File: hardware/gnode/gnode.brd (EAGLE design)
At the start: 50 x 35 mm, 8 parts, among them U1 ATMEGA328P_TQFP, U2 3.3V/150mA

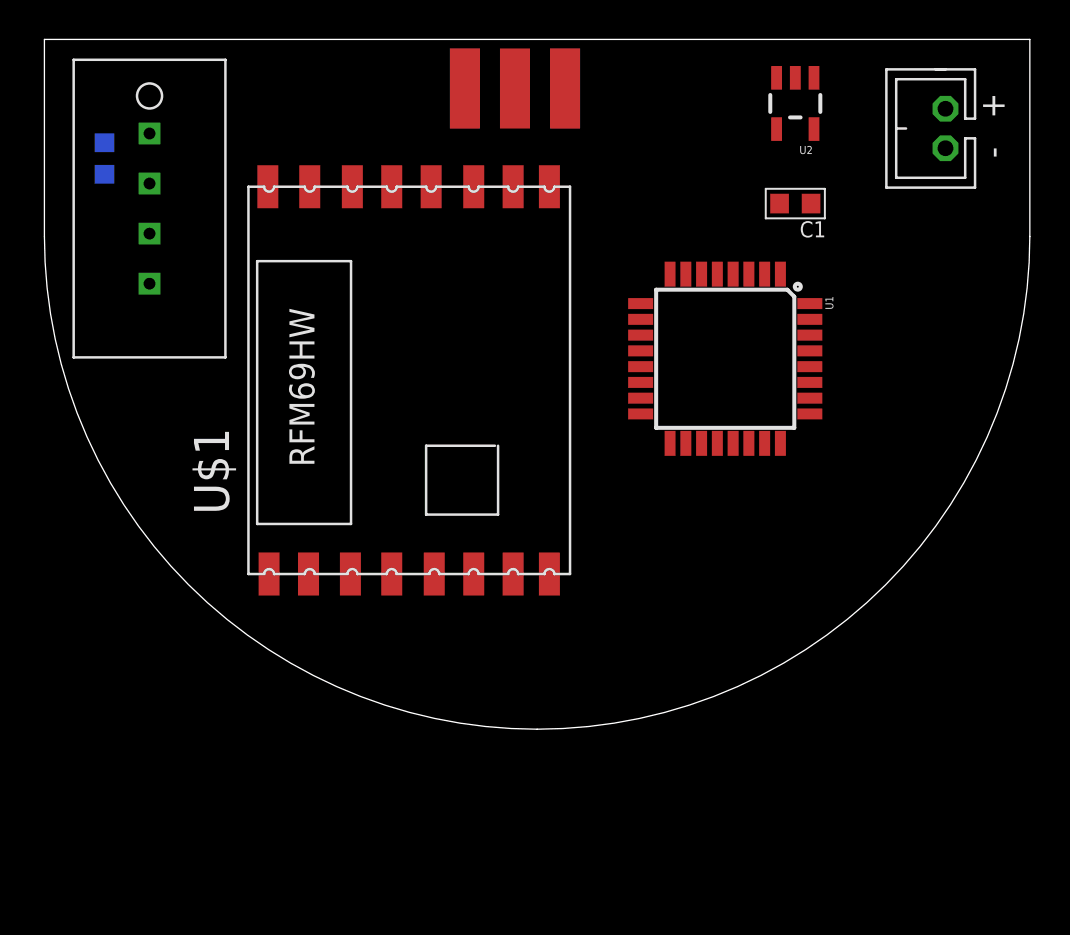
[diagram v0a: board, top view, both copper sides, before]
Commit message: reduced to r25mm, added htu21d and icsp header
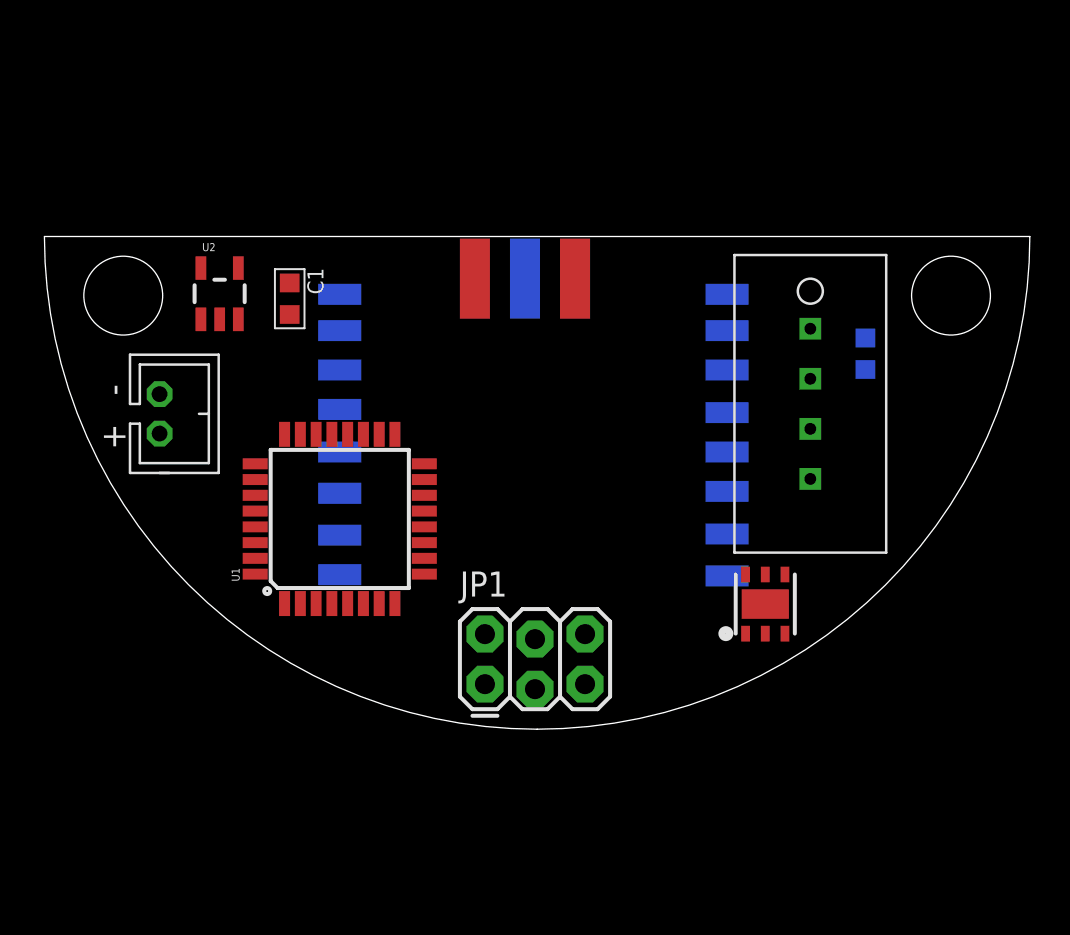
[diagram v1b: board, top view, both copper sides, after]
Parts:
- added IC1: HTU21D, Mine:DFN6-L
- added JP1: AVR_SPI_PRG_62X3_LOCK, SparkFun-Connectors:2X3_LOCK
- moved J1 42.4 mm to (5.84, 16.0), turned to 270 degrees
- moved R1 39.9 mm to (41.7, 19.1)
- moved U$2 35.0 mm to (38.9, 16.5)
- moved U2 30.8 mm to (8.89, 22.1), turned to 0 degrees
- moved C1 26.1 mm to (12.4, 21.8), turned to 270 degrees
- moved U1 21.2 mm to (15.0, 10.7), turned to 90 degrees
- moved U$1 19.2 mm to (15.0, 23.1), flipped to the bottom, turned to 180 degrees
- moved J$1 11.2 mm to (26.9, 22.9), flipped to the bottom
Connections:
- new net NRST: JP1.5, U1.29
- new net SHT_DATA: IC1.1, U1.27
- new net SHT_SCK: IC1.6, U1.28
- net GND: now also IC1.2, JP1.6
- net MISO: now also JP1.1
- net MOSI: now also JP1.4
- net SCK: now also JP1.3
- net VCC: now also JP1.2
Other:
- board size 50 x 35 mm -> 50 x 25 mm

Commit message: switched to mcp1700
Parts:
- removed U2: 3.3V/150mA, SparkFun-PowerIC:SOT23-5
- added C2: 1u, passives-7351:C0603-N
- added U$3: MCP1700TT, dtb:SOT23
- C1: value (none) -> 1u
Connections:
- net GND: now also C2.2, U$3.1; no longer U2.2
- net N$2: now also C2.1, U$3.3; no longer U2.1, U2.3
- net VCC: now also U$3.2; no longer U2.5
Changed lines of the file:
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@@
 <element name="R1" library="passives-7351" package="R0603-N" value="" x="41.656" y="19.05" rot="MR90"/>
 <element name="J1" library="dtb" package="JST-2-TH" value="" x="5.842" y="16.002" rot="R270"/>
-<element name="U2" library="SparkFun-PowerIC" package="SOT23-5" value="3.3V/150mA" x="8.89" y="22.098">
-<attribute name="PROD_ID" value="VREG-00822" x="8.89" y="22.098" size="1.778" layer="27" font="vector" ratio="15" display="off"/>
-</element>
-<element name="C1" library="passives-7351" package="C0603-N" value="" x="12.446" y="21.844" rot="R270"/>
+<element name="C1" library="passives-7351" package="C0603-N" value="1u" x="12.446" y="21.844" rot="R270"/>
 <element name="IC1" library="Mine" package="DFN6-L" value="HTU21D" x="36.576" y="6.35"/>
 <element name="JP1" library="SparkFun-Connectors" package="2X3_LOCK" value="AVR_SPI_PRG_62X3_LOCK" x="22.352" y="2.286"/>
+<element name="U$3" library="dtb" package="SOT23" value="MCP1700TT" x="8.89" y="21.844" rot="R90"/>
+<element name="C2" library="passives-7351" package="C0603-N" value="1u" x="11.43" y="19.05"/>
 </elements>
 <signals>
@@
 <contactref element="U1" pad="21"/>
 <contactref element="J1" pad="2"/>
-<contactref element="U2" pad="2"/>
 <contactref element="C1" pad="2"/>
 <contactref element="IC1" pad="2"/>
 <contactref element="JP1" pad="6"/>
+<contactref element="U$3" pad="1"/>
+<contactref element="C2" pad="2"/>
 <wire x1="34.63725" y1="18.22525" x2="34.63725" y2="22.0665" width="0" layer="19" extent="16-16"/>
 <wire x1="38.862" y1="12.7" x2="34.63725" y2="18.22525" width="0" layer="19" extent="16-16"/>
@@
 <wire x1="27.432" y1="4.826" x2="36.576" y2="4.85" width="0" layer="19" extent="1-1"/>
 <wire x1="12.446" y1="21.044" x2="21.844" y2="22.86" width="0" layer="19" extent="1-1"/>
-<wire x1="8.89" y1="20.7979" x2="12.446" y2="21.044" width="0" layer="19" extent="1-1"/>
-<wire x1="5.842" y1="17.002" x2="8.89" y2="20.7979" width="0" layer="19" extent="1-1"/>
-<wire x1="14.586" y1="14.9606" x2="12.446" y2="21.044" width="0" layer="19" extent="1-1"/>
+<wire x1="12.23" y1="19.05" x2="12.446" y2="21.044" width="0" layer="19" extent="1-1"/>
+<wire x1="9.99" y1="20.894" x2="12.446" y2="21.044" width="0" layer="19" extent="1-1"/>
+<wire x1="14.586" y1="14.9606" x2="12.23" y2="19.05" width="0" layer="19" extent="1-1"/>
+<wire x1="5.842" y1="17.002" x2="9.99" y2="20.894" width="0" layer="19" extent="1-1"/>
 <wire x1="15.386" y1="6.3754" x2="14.586" y2="14.9606" width="0" layer="19" extent="1-1"/>
 <wire x1="13.786" y1="6.3754" x2="15.386" y2="6.3754" width="0" layer="19" extent="1-1"/>
@@
 <contactref element="U1" pad="4"/>
 <contactref element="U1" pad="6"/>
-<contactref element="U2" pad="5"/>
 <contactref element="C1" pad="1"/>
 <contactref element="JP1" pad="2"/>
+<contactref element="U$3" pad="2"/>
 <wire x1="12.446" y1="22.644" x2="14.986" y2="22.0665" width="0" layer="19" extent="1-16"/>
-<wire x1="7.94" y1="23.3981" x2="12.446" y2="22.644" width="0" layer="19" extent="1-1"/>
+<wire x1="9.99" y1="22.794" x2="12.446" y2="22.644" width="0" layer="19" extent="1-1"/>
 <wire x1="16.986" y1="14.9606" x2="14.986" y2="22.0665" width="0" layer="19" extent="1-16"/>
 <wire x1="16.186" y1="6.3754" x2="16.986" y2="14.9606" width="0" layer="19" extent="1-1"/>
@@
 </signal>
 <signal name="N$2">
-<contactref element="U2" pad="1"/>
 <contactref element="J1" pad="1"/>
-<contactref element="U2" pad="3"/>
-<wire x1="9.84" y1="20.7979" x2="7.94" y2="20.7979" width="0" layer="19" extent="1-1"/>
-<wire x1="5.842" y1="15.002" x2="7.94" y2="20.7979" width="0" layer="19" extent="1-1"/>
+<contactref element="U$3" pad="3"/>
+<contactref element="C2" pad="1"/>
+<wire x1="10.63" y1="19.05" x2="7.79" y2="21.844" width="0" layer="19" extent="1-1"/>
+<wire x1="5.842" y1="15.002" x2="10.63" y2="19.05" width="0" layer="19" extent="1-1"/>
 </signal>
 <signal name="SHT_SCK">

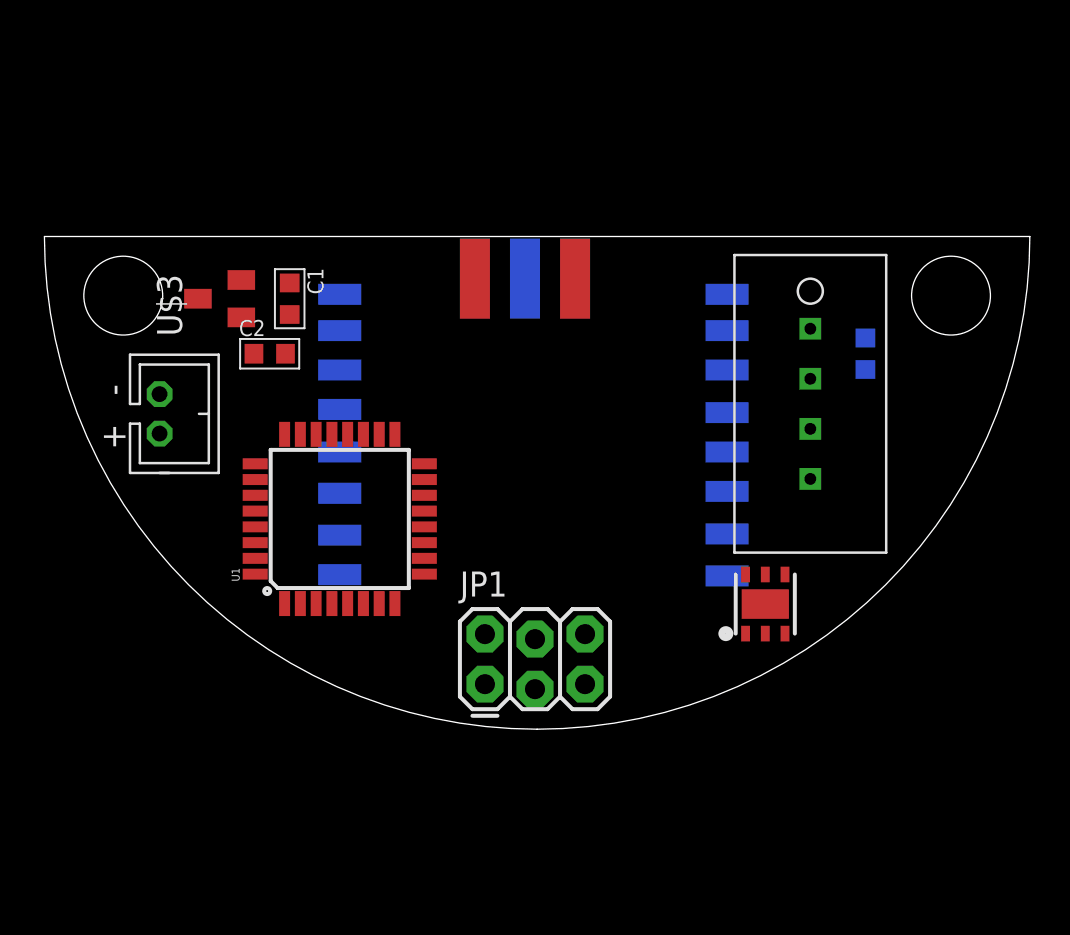
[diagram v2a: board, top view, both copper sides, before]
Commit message: added cn3083 solar charger
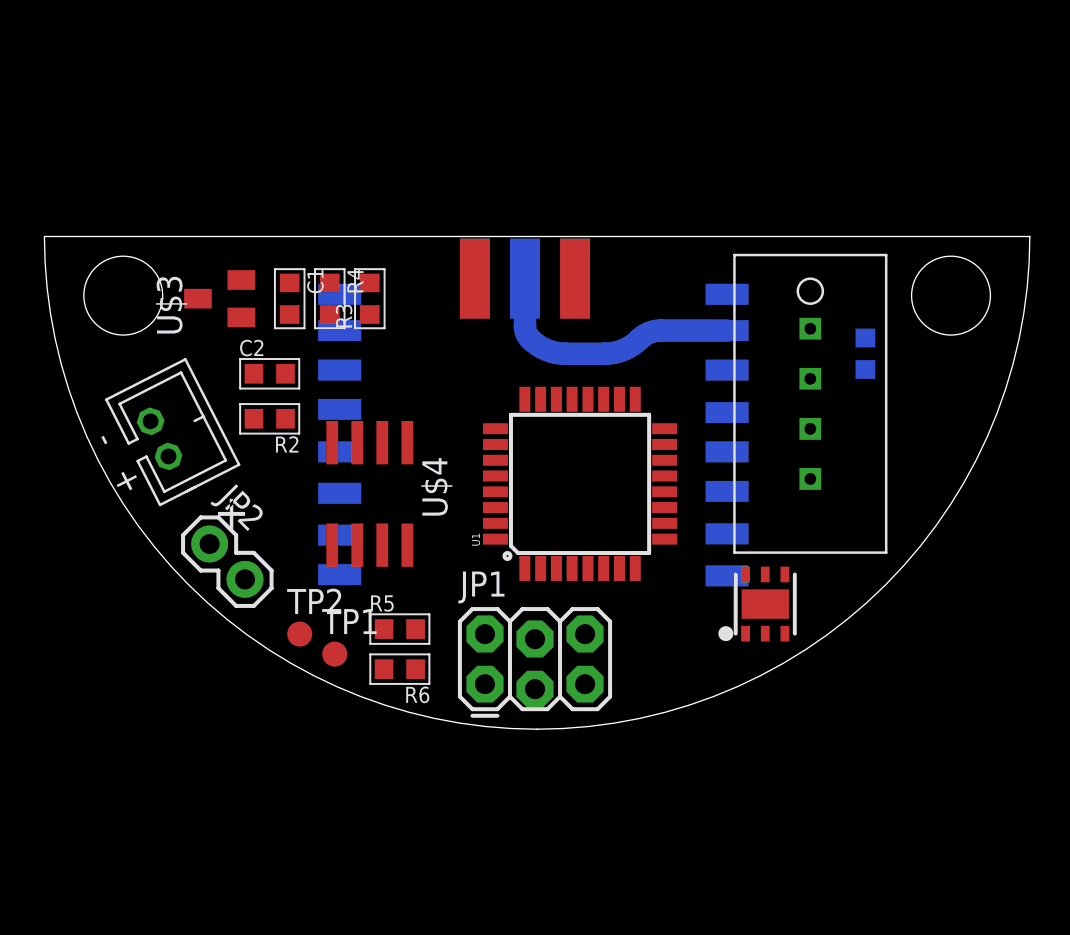
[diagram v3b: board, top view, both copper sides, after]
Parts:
- added JP2: (no value), Mine:1X02
- added R2: 3k6, passives-7351:R0603-N
- added R3, R4, R5, R6: 100k, passives-7351:R0603-N
- added TP1, TP2: PTR1B1,27, testpad:B1,27
- added U$4: CN3083, jonsowman:SOIC8
- moved U1 12.3 mm to (27.2, 12.4)
- moved J1 1.27 mm to (5.84, 14.7), turned to 297 degrees
- moved C2 1.02 mm to (11.4, 18.0)
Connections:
- new net N$3: JP2.1, U$4.4
- new net N$4: R2.2, U$4.2
- new net N$5: R6.2, TP2.TP, U$4.6
- new net VBATT: C2.1, J1.1, U$3.3, U$4.5, U$4.8
- new net VSENSE: R3.1, R4.2, U1.23
- net GND: now also JP2.2, R2.1, R4.1, U$4.1, U$4.3
- net N$2: now also R5.1, TP1.TP, U$4.7; no longer C2.1, J1.1, U$3.3
- net VCC: now also R3.2, R5.2, R6.1
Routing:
- net N$1: track 0.00 -> 13.5 mm
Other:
- board text added: "+"

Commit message: sense panel and battery voltages
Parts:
- added R7, R8: 100k, passives-7351:R0603-N
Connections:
- net VSENSE renamed VSENSE_BATT
- removed net N$3: JP2.1, U$4.4
- new net VPANEL: JP2.1, R7.2, U$4.4
- new net VSENSE_PANEL: R7.1, R8.2, U1.24
- net GND: now also R8.1
- net VBATT: now also R3.2
- net VCC: no longer R3.2
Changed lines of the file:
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@@
 <setting verticaltext="up"/>
 </settings>
-<grid distance="0.01" unitdist="inch" unit="inch" style="lines" multiple="1" display="yes" altdistance="0.005" altunitdist="inch" altunit="inch"/>
+<grid distance="0.05" unitdist="inch" unit="inch" style="lines" multiple="1" display="yes" altdistance="0.005" altunitdist="inch" altunit="inch"/>
 <layers>
 <layer number="1" name="Top" color="4" fill="1" visible="yes" active="yes"/>
@@
 <element name="R5" library="passives-7351" package="R0603-N" value="100k" x="18.034" y="5.08"/>
 <element name="R6" library="passives-7351" package="R0603-N" value="100k" x="18.034" y="3.048" rot="R180"/>
+<element name="R7" library="passives-7351" package="R0603-N" value="100k" x="2.54" y="-3.81"/>
+<element name="R8" library="passives-7351" package="R0603-N" value="100k" x="2.54" y="-7.62"/>
 </elements>
 <signals>
@@
 <contactref element="U$4" pad="1"/>
 <contactref element="R4" pad="1"/>
+<contactref element="R8" pad="1"/>
 <wire x1="34.63725" y1="18.22525" x2="34.63725" y2="22.0665" width="0" layer="19" extent="16-16"/>
 <wire x1="38.862" y1="12.7" x2="34.63725" y2="18.22525" width="0" layer="19" extent="16-16"/>
@@
 <wire x1="25.978" y1="8.1534" x2="27.578" y2="8.1534" width="0" layer="19" extent="1-1"/>
 <wire x1="27.432" y1="4.826" x2="27.578" y2="8.1534" width="0" layer="19" extent="1-1"/>
+<wire x1="1.74" y1="-7.62" x2="10.17805" y2="7.601946875" width="0" layer="19" extent="1-1"/>
 </signal>
 <signal name="N$1">
@@
 <contactref element="JP1" pad="2"/>
 <contactref element="U$3" pad="2"/>
-<contactref element="R3" pad="2"/>
 <contactref element="R5" pad="2"/>
 <contactref element="R6" pad="1"/>
@@
 <wire x1="18.834" y1="5.08" x2="22.352" y2="4.826" width="0" layer="19" extent="1-1"/>
 <wire x1="18.834" y1="3.048" x2="18.834" y2="5.08" width="0" layer="19" extent="1-1"/>
-<wire x1="16.51" y1="22.644" x2="29.178" y2="16.7386" width="0" layer="19" extent="1-1"/>
-<wire x1="14.986" y1="22.0665" x2="16.51" y2="22.644" width="0" layer="19" extent="1-16"/>
+<wire x1="14.986" y1="22.0665" x2="29.178" y2="16.7386" width="0" layer="19" extent="1-16"/>
 <wire x1="12.446" y1="22.644" x2="14.986" y2="22.0665" width="0" layer="19" extent="1-16"/>
 <wire x1="9.99" y1="22.794" x2="12.446" y2="22.644" width="0" layer="19" extent="1-1"/>
@@
 <contactref element="U$4" pad="5"/>
 <contactref element="U$4" pad="8"/>
-<wire x1="10.63" y1="18.034" x2="7.79" y2="21.844" width="0" layer="19" extent="1-1"/>
+<contactref element="R3" pad="2"/>
+<wire x1="10.63" y1="18.034" x2="16.51" y2="22.644" width="0" layer="19" extent="1-1"/>
+<wire x1="7.79" y1="21.844" x2="10.63" y2="18.034" width="0" layer="19" extent="1-1"/>
 <wire x1="6.2959875" y1="13.840990625" x2="10.63" y2="18.034" width="0" layer="19" extent="1-1"/>
 <wire x1="14.605" y1="9.338" x2="6.2959875" y2="13.840990625" width="0" layer="19" extent="1-1"/>
@@
 <wire x1="27.432" y1="2.286" x2="22.8854" y2="12.046" width="0" layer="19" extent="1-1"/>
 </signal>
-<signal name="N$3">
-<contactref element="JP2" pad="1"/>
-<contactref element="U$4" pad="4"/>
-<wire x1="8.382" y1="9.398" x2="14.605" y2="14.538" width="0" layer="19" extent="1-1"/>
-</signal>
 <signal name="N$4">
 <contactref element="U$4" pad="2"/>
 <contactref element="R2" pad="2"/>
 <wire x1="10.63" y1="15.748" x2="17.145" y2="14.538" width="0" layer="19" extent="1-1"/>
-</signal>
-<signal name="VSENSE">
-<contactref element="U1" pad="23"/>
-<contactref element="R3" pad="1"/>
-<contactref element="R4" pad="2"/>
-<wire x1="16.51" y1="21.044" x2="25.178" y2="16.7386" width="0" layer="19" extent="1-1"/>
-<wire x1="14.478" y1="21.044" x2="16.51" y2="21.044" width="0" layer="19" extent="1-1"/>
 </signal>
 <signal name="N$2">
@@
 <wire x1="17.234" y1="3.048" x2="12.954" y2="4.826" width="0" layer="19" extent="1-1"/>
 </signal>
+<signal name="VPANEL">
+<contactref element="JP2" pad="1"/>
+<contactref element="U$4" pad="4"/>
+<contactref element="R7" pad="2"/>
+<wire x1="8.382" y1="9.398" x2="14.605" y2="14.538" width="0" layer="19" extent="1-1"/>
+<wire x1="3.34" y1="-3.81" x2="8.382" y2="9.398" width="0" layer="19" extent="1-1"/>
+</signal>
+<signal name="VSENSE_BATT">
+<contactref element="R3" pad="1"/>
+<contactref element="R4" pad="2"/>
+<contactref element="U1" pad="23"/>
+<wire x1="16.51" y1="21.044" x2="25.178" y2="16.7386" width="0" layer="19" extent="1-1"/>
+<wire x1="14.478" y1="21.044" x2="16.51" y2="21.044" width="0" layer="19" extent="1-1"/>
+</signal>
+<signal name="VSENSE_PANEL">
+<contactref element="U1" pad="24"/>
+<contactref element="R7" pad="1"/>
+<contactref element="R8" pad="2"/>
+<wire x1="1.74" y1="-3.81" x2="24.378" y2="16.7386" width="0" layer="19" extent="1-1"/>
+<wire x1="3.34" y1="-7.62" x2="1.74" y2="-3.81" width="0" layer="19" extent="1-1"/>
+</signal>
 </signals>
